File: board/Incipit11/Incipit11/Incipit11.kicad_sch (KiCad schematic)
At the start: 35 parts, among them J1 SM04B-SRSS-TB_LF__SN_, J2 Conn_01x03, J3 Conn_02x03_Odd_Even, J4 Conn_01x02, J5 284391-6, Q1 MCU30N02-TP, SW1 SW_Push, U1 ATTINY3224-XUR, U2 EL0631(TA), U3 SPX1117M3-L-3-3/TR

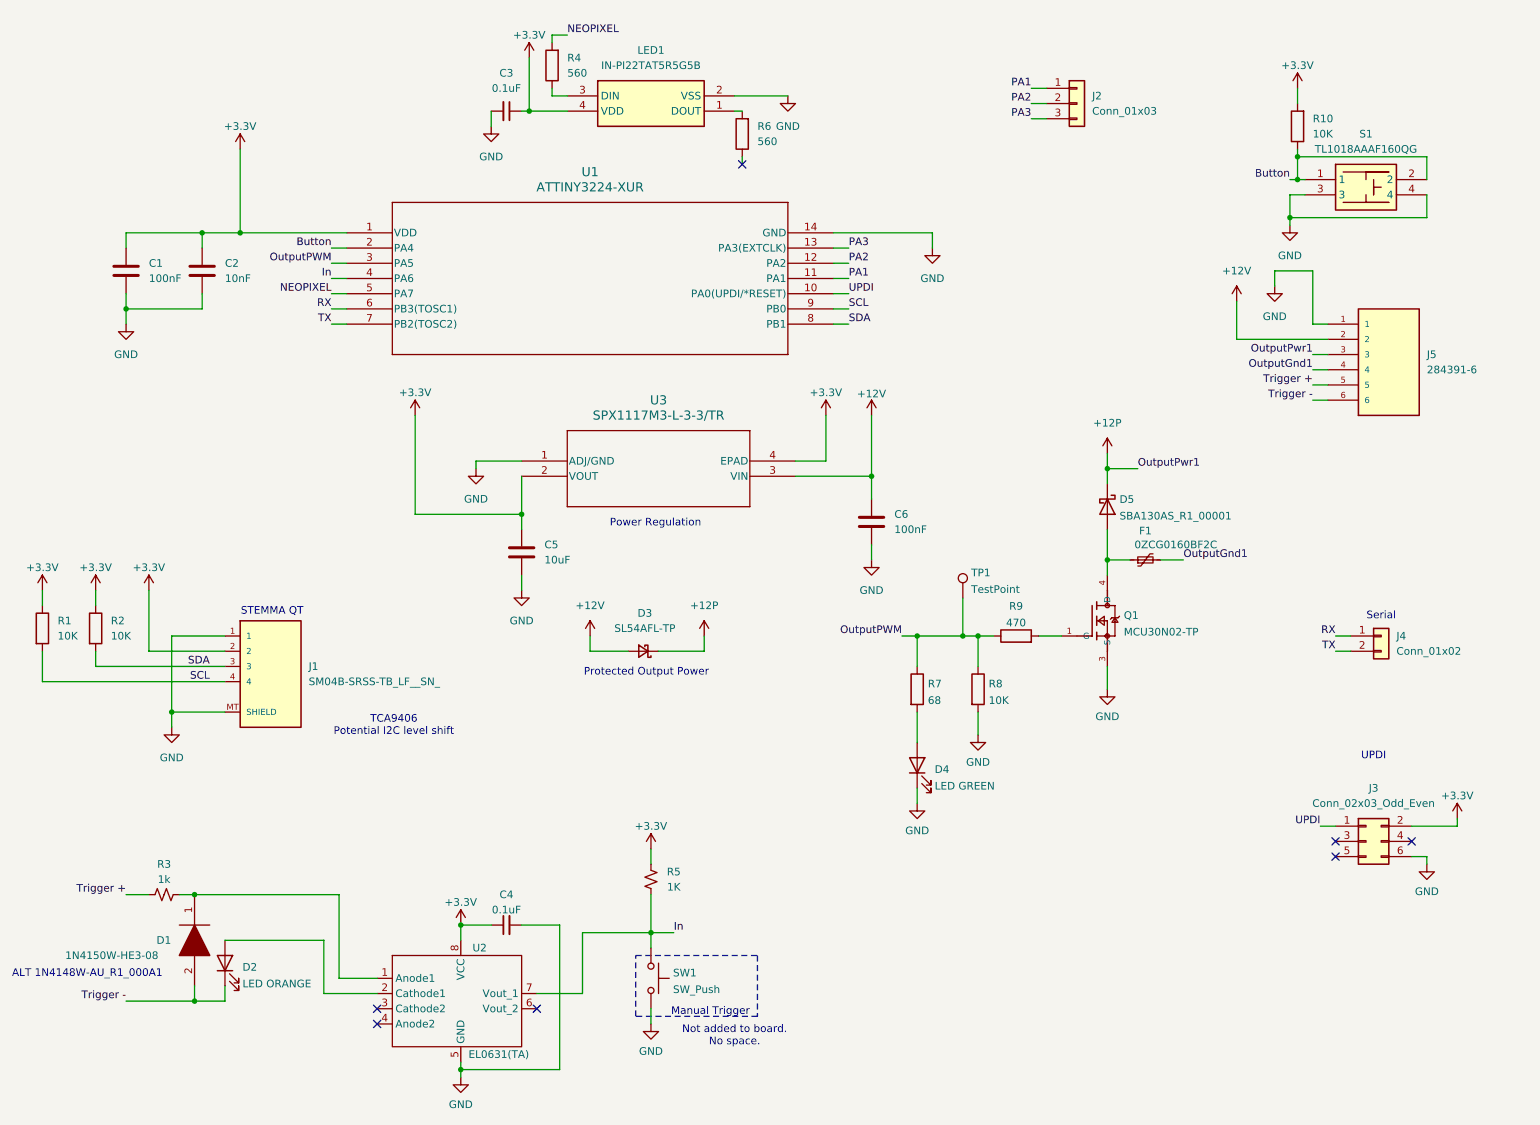
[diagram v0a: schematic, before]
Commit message: Rev B of board for new case. Did a few modifications to add more reverse protection on output and changed the I2C to seperate the 3.3 power from controller and peripheral.
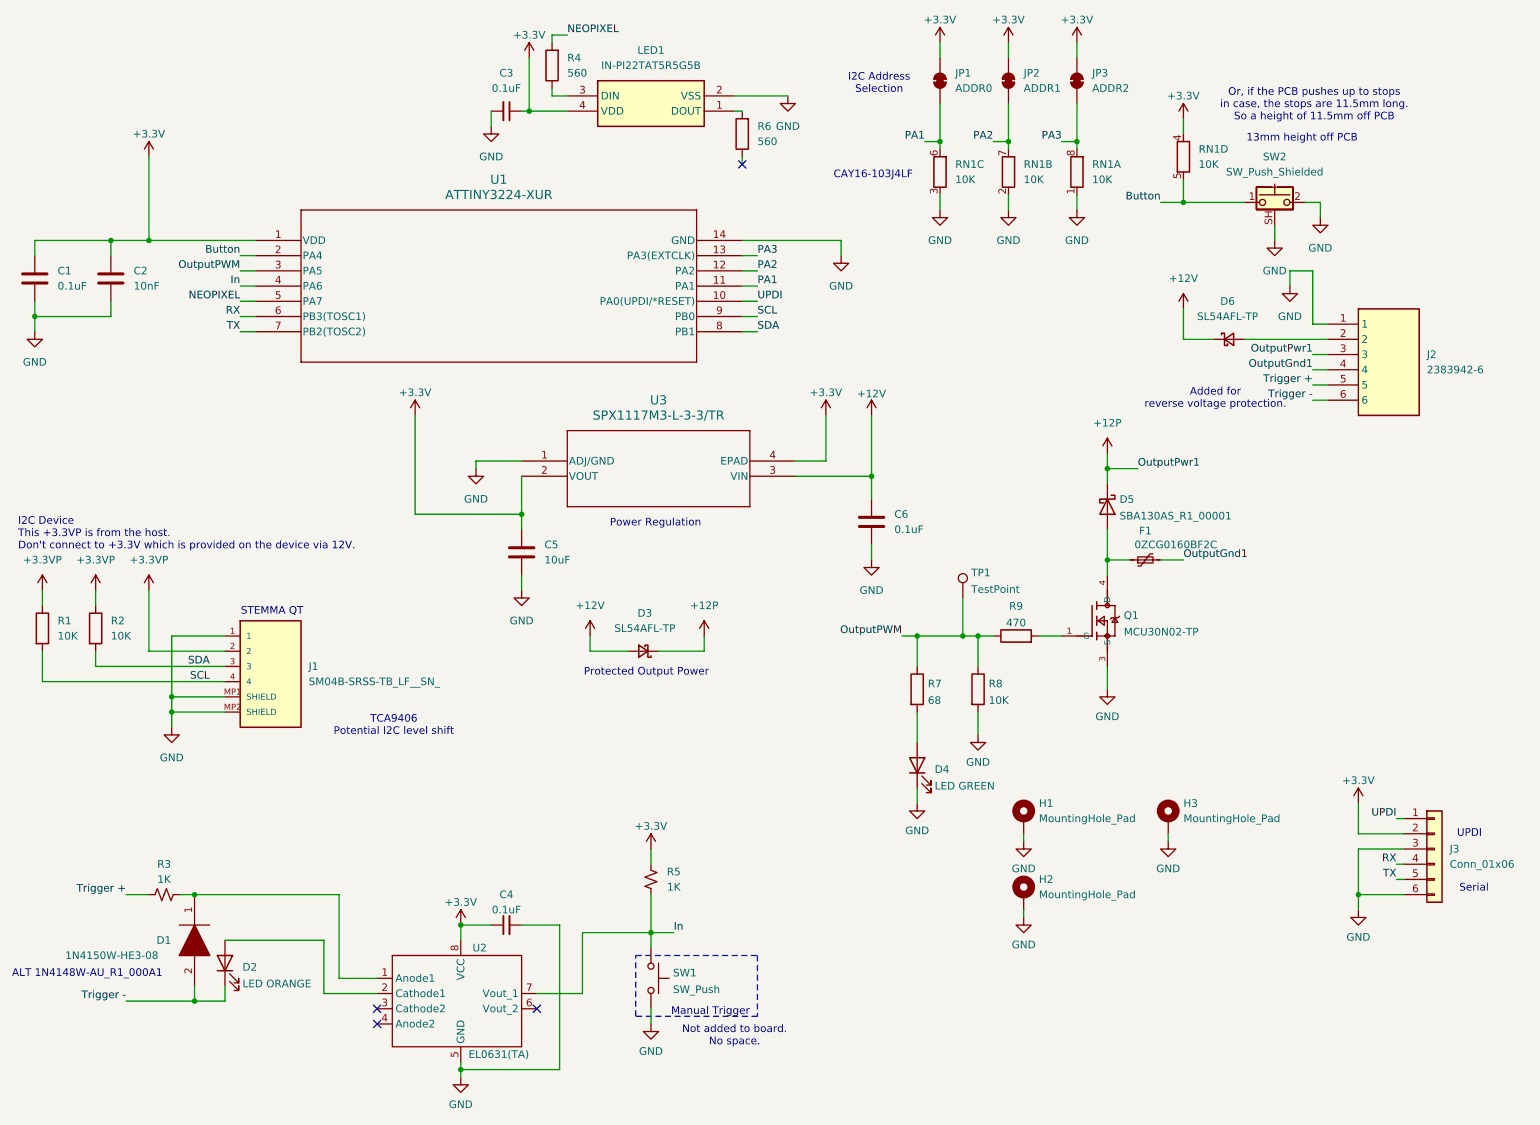
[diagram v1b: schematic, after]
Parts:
- removed J2: Conn_01x03, Connector_PinHeader_2.54mm:PinHeader_1x03_P2.54mm_Vertical, symbol Connector_Generic:Conn_01x03
- removed J3: Conn_02x03_Odd_Even, Connector_PinHeader_2.54mm:PinHeader_2x03_P2.54mm_Vertical, symbol Connector_Generic:Conn_02x03_Odd_Even
- removed J4: Conn_01x02, Connector_PinHeader_2.54mm:PinHeader_1x02_P2.54mm_Vertical, symbol Connector_Generic:Conn_01x02
- removed J5: 284391-6, Department of Alchemy:TE_284391-6, symbol Department of Alchemy:284391-6
- removed R10: 10K, Resistor_SMD:R_0603_1608Metric, symbol Device:R
- removed S1: TL1018AAAF160QG, Department of Alchemy:TL1018AAAF160QG, symbol Department of Alchemy:TL1018AAAF160QG
- added D6: SL54AFL-TP, Department of Alchemy:SL54AFL-TP DO-221AC(SMA-FL), symbol Department of Alchemy:SK54A-LTP
- added H1, H2, H3: MountingHole_Pad, MountingHole:MountingHole_2.2mm_M2_ISO7380_Pad_TopBottom, symbol Mechanical:MountingHole_Pad
- added J2: 2383942-6, Department of Alchemy:393570006, symbol Department of Alchemy:2383942-6
- added J3: Conn_01x06, Connector_PinHeader_2.54mm:PinHeader_1x06_P2.54mm_Vertical, symbol Connector_Generic:Conn_01x06
- added JP1: ADDR0, Jumper:SolderJumper-2_P1.3mm_Bridged_RoundedPad1.0x1.5mm, symbol Jumper:SolderJumper_2_Bridged
- added JP2: ADDR1, Jumper:SolderJumper-2_P1.3mm_Bridged_RoundedPad1.0x1.5mm, symbol Jumper:SolderJumper_2_Bridged
- added JP3: ADDR2, Jumper:SolderJumper-2_P1.3mm_Bridged_RoundedPad1.0x1.5mm, symbol Jumper:SolderJumper_2_Bridged
- added RN1: 10K, Resistor_SMD:R_Array_Convex_4x0603, symbol Device:R_Pack04_Split
- added SW2: SW_Push_Shielded, Department of Alchemy:CT1102P, symbol Switch:SW_Push_Shielded
- C1, C6: value 100nF -> 0.1uF
- J1: footprint Department of Alchemy:JST_SH_SM04B-SRSS-TB_1x04-1MP_P1.00mm_Horizontal -> Department of Alchemy:JST_SH_BM04B-SRSS-TB_1x04-1MP_P1.00mm_Vertical
- R3: value 1k -> 1K
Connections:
- net +12P: now also J2.3
- net +12V: now also D6.1 (K)
- net +3.3V: now also J3.2 (Pin_2), JP1.2 (B), JP2.2 (B), JP3.2 (B), RN1.4 (R4.1); no longer J1.2, R1.1, R2.1
- net Button: now also RN1.5 (R4.2), SW2.1
- net GND: now also J1.MP1 (SHIELD), J1.MP2 (SHIELD), H1.1, H2.1, H3.1, J2.1, J3.3 (Pin_3), J3.6 (Pin_6), RN1.1 (R1.1), RN1.2 (R2.1), RN1.3 (R3.1), SW2.2, SW2.SH (B); no longer J1.MT (SHIELD)
- net OutputGnd1: now also J2.4
- net PA1: now also JP1.1 (A), RN1.6 (R3.2)
- net PA2: now also JP2.1 (A), RN1.7 (R2.2)
- net PA3: now also JP3.1 (A), RN1.8 (R1.2)
- net RX: now also J3.4 (Pin_4)
- net TX: now also J3.5 (Pin_5)
- net Trigger +: now also J2.5
- net Trigger -: now also J2.6
- net UPDI: now also J3.1 (Pin_1)
- new net: D6.2 (A), J2.2
- new net +3.3VP: J1.2, R1.1, R2.1
- no-connect marks 7 -> 4
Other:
- note added: "13mm height off PCB"
- note added: "Added for reverse voltage protection."
- note added: "CAY16-103J4LF"
- note added: "I2C Address Selection"
- note added: "I2C Device This +3.3VP is from the host. Don't connect to +3.3V which is provided on the device via 12V."
- note added: "Or, if the PCB pushes up to stops in case, the stops are 11.5mm long. So a height of 11.5mm off PCB"
- moved on the sheet: C1, C2, U1
